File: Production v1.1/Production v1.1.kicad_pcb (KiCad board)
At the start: 2 copper layers, 35 x 30.2 mm, 39 parts, among them IC1 MAX3323EEUE+T, IC2 AP7375-33SA-7, J1 530480510, J13 FH34SRJ-16S-0.5SH_50_, J2 530480410, J3 USB4085-GF-A_REVB, U2 ADR02AUJZ-REEL7, U3 ATSAMD21G18A-AUT, Y1 ECS-.327-12.5-1210-TR

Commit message: Better v1.1, but I can do better
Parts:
- C13, C4, D1, D2, IC2: moved to B.Cu
- R1: moved to F.Cu
- RESET1: footprint Button_Switch_SMD:SW_SPST_B3U-1000P -> Button_Switch_SMD:SW_SPST_B3U-3000P
- moved J1 30.9 mm to (90.7, 90.2), turned to 90 degrees
- moved C3 29.1 mm to (119.5, 92.0), turned to 0 degrees
- moved J2 28.3 mm to (122.2, 85.2), turned to -90 degrees
- moved C1 28.3 mm to (120.5, 90.5), turned to 90 degrees
- moved C2 27.3 mm to (117.5, 92.0), turned to 180 degrees
- moved C5 25.8 mm to (115.5, 92.0), turned to 180 degrees
- moved U2 25.8 mm to (94.5, 88.8), turned to 90 degrees
- moved IC1 22.3 mm to (117.2, 87.5), turned to 90 degrees
- moved C4 15.3 mm to (112.8, 88.5), turned to 180 degrees
- moved D2 14.3 mm to (112.0, 92.0), turned to -90 degrees
- moved IC2 13.6 mm to (112.5, 85.8), turned to 0 degrees
- moved R3 11.0 mm to (101.0, 79.0)
- moved R5 11.0 mm to (101.0, 77.4)
- moved 3V3 11.0 mm to (128.8, 79.2)
- moved SWCLK 11.0 mm to (123.7, 79.2)
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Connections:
- U3 pad 16: unconnected-(U3-PA11-Pad16) -> ZSIG
- U3 pad 24: unconnected-(U3-PA15-Pad24) -> RUN
- U3 pad 39: RUN -> unconnected-(U3-PA27-Pad39)
- U3 pad 47: ZSIG -> unconnected-(U3-PB02-Pad47)
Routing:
- net GND: track 66.7 -> 15.8 mm, vias 20 -> 14
- net +3V3: track 66.3 -> 38.7 mm, vias 3 -> 1
- net SWDIO: track 14.0 -> 0.00 mm, vias 1 -> 0
- net SWCLK: track 10.1 -> 0.00 mm, vias 1 -> 0
- net +24V: track 38.5 -> 46.7 mm
- net Net-(J13-Pad4): track 8.50 -> 1.88 mm
- net RST: track 14.3 -> 20.6 mm
- net VIN: track 9.08 -> 4.18 mm
- net /Net-(J8-CC1): track 1.30 -> 5.67 mm
- net TIN1: track 8.97 -> 13.2 mm
- net SETBTN: track 19.0 -> 16.4 mm, vias 1 -> 0
- net VUSB: track 13.8 -> 11.9 mm
- net ROUT1: track 9.27 -> 11.2 mm
- net TOUT1: track 9.65 -> 8.29 mm
- net ZOOM: track 16.9 -> 15.6 mm
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- added copper zone on F.Cu, net GND
- added copper zone on B.Cu, net VIN
- removed copper zone on F.Cu, net VIN

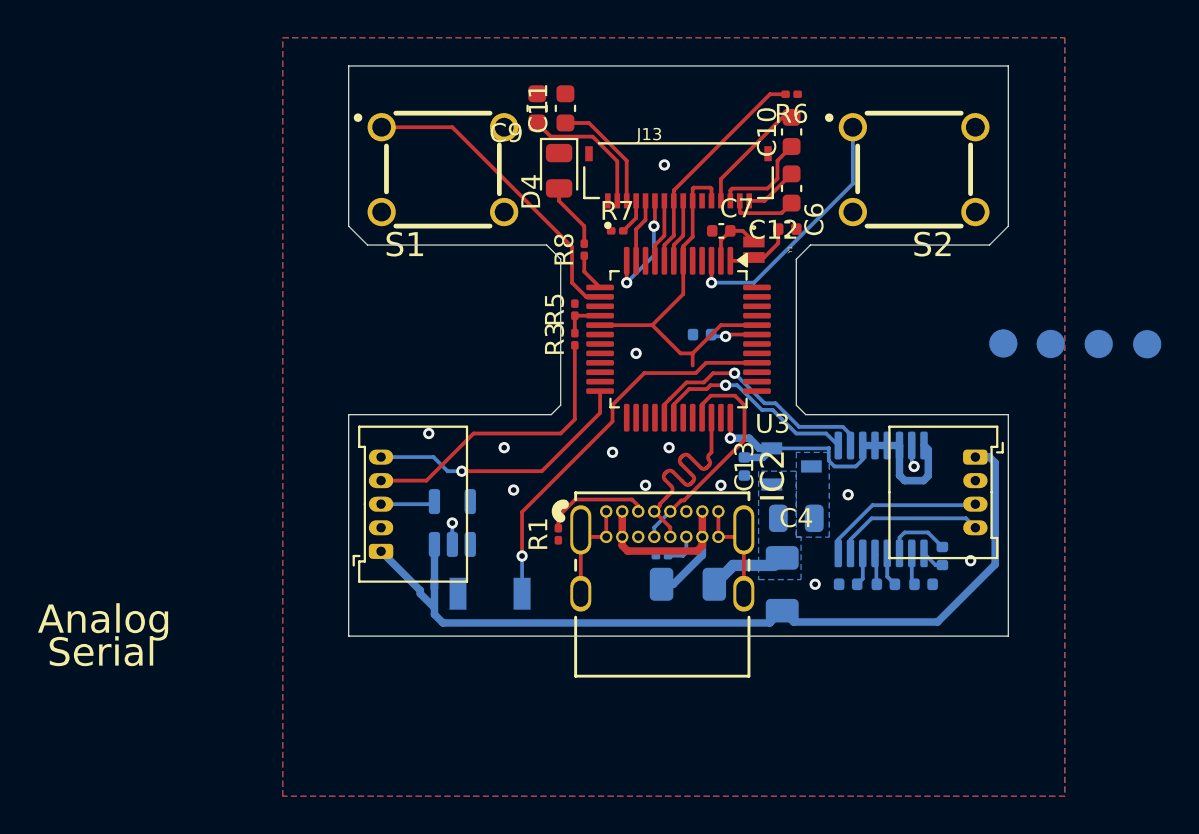
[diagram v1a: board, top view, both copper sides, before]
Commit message: Components are all moved to the bottom layer, top is ground
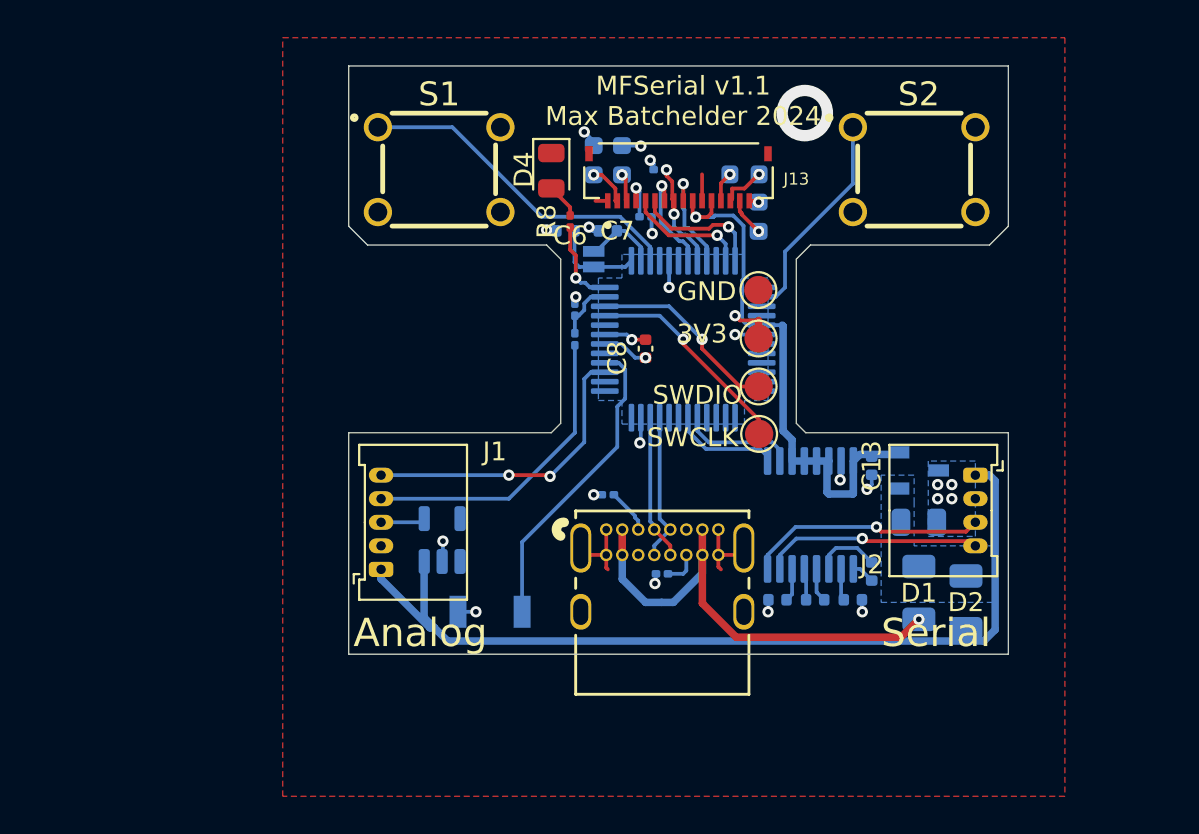
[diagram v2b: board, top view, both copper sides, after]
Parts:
- 3V3, C8, SWCLK, SWDIO: moved to F.Cu
- C10, C11, C12, C6, C7, C9, R1, R3, R5, R6, R7, U3, Y1: moved to B.Cu
- GND: renamed from G; moved to F.Cu
- moved GND 20.8 mm to (110.7, 76.4), turned to 0 degrees
- moved 3V3 18.0 mm to (110.8, 79.0), turned to 0 degrees
- moved SWDIO 15.7 mm to (110.8, 81.5), turned to 0 degrees
- moved SWCLK 13.8 mm to (110.8, 84.0), turned to 0 degrees
- moved D1 12.3 mm to (119.2, 92.5), turned to -90 degrees
- moved C6 11.8 mm to (100.5, 73.2), turned to 0 degrees
- moved D2 9.80 mm to (121.8, 93.0)
- moved Y1 8.51 mm to (102.0, 74.8)
- moved R6 8.06 mm to (105.5, 70.0), turned to 0 degrees
- moved IC2 6.75 mm to (119.2, 86.0)
- moved C13 6.75 mm to (116.8, 85.7)
- moved C4 6.50 mm to (119.2, 88.7)
- moved C7 6.02 mm to (102.8, 73.2)
- moved C11 4.07 mm to (103.5, 69.5)
- moved C9 4.07 mm to (102.0, 69.5)
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- renumbered RESET1 to S3
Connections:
- U3 pad 13: SETLED -> unconnected-(U3-PA08-Pad13)
- U3 pad 14: SETBTN -> SOFTBTN
- U3 pad 16: ZSIG -> unconnected-(U3-PA11-Pad16)
- U3 pad 24: RUN -> unconnected-(U3-PA15-Pad24)
- U3 pad 3: SOFTBTN -> SETBTN
- U3 pad 39: unconnected-(U3-PA27-Pad39) -> RUN
- U3 pad 47: unconnected-(U3-PB02-Pad47) -> ZSIG
- U3 pad 48: RXLED -> SETLED
- U3 pad 7: OLED_CS -> OLED_DC
- U3 pad 9: OLED_DC -> OLED_CS
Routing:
- net VUSB: track 11.9 -> 25.5 mm, vias 0 -> 1
- net GND: track 15.8 -> 27.2 mm, vias 14 -> 23
- net SWCLK: track 0.00 -> 11.4 mm, vias 0 -> 1
- net SWDIO: track 0.00 -> 10.2 mm, vias 0 -> 1
- net TIN1: track 13.2 -> 6.08 mm, vias 1 -> 0
- net OLED_RST: track 12.0 -> 5.66 mm, vias 0 -> 2
- net +3V3: track 38.7 -> 33.1 mm, vias 1 -> 2
- net ROUT1: track 11.2 -> 5.73 mm, vias 1 -> 0
- net Net-(C9-Pad2): track 7.19 -> 2.20 mm, vias 0 -> 1
- net Net-(C11-Pad1): track 6.21 -> 1.49 mm, vias 0 -> 1
- net Net-(C10-Pad2): track 6.26 -> 1.60 mm, vias 0 -> 1
- net D+: track 12.3 -> 7.72 mm
- net D-: track 12.4 -> 7.87 mm
- net RST: track 20.6 -> 16.4 mm, vias 1 -> 0
- net VIN: track 4.18 -> 0.00 mm
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- added copper zone on B.Cu, net +3V3
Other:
- board size 35 x 30.2 mm -> 35 x 31.2 mm
- board text added: "MFSerial v1.1 Max Batchelder 2024"
- board text removed: "MFSerial Production v1.1 Max Batchelder 2024"

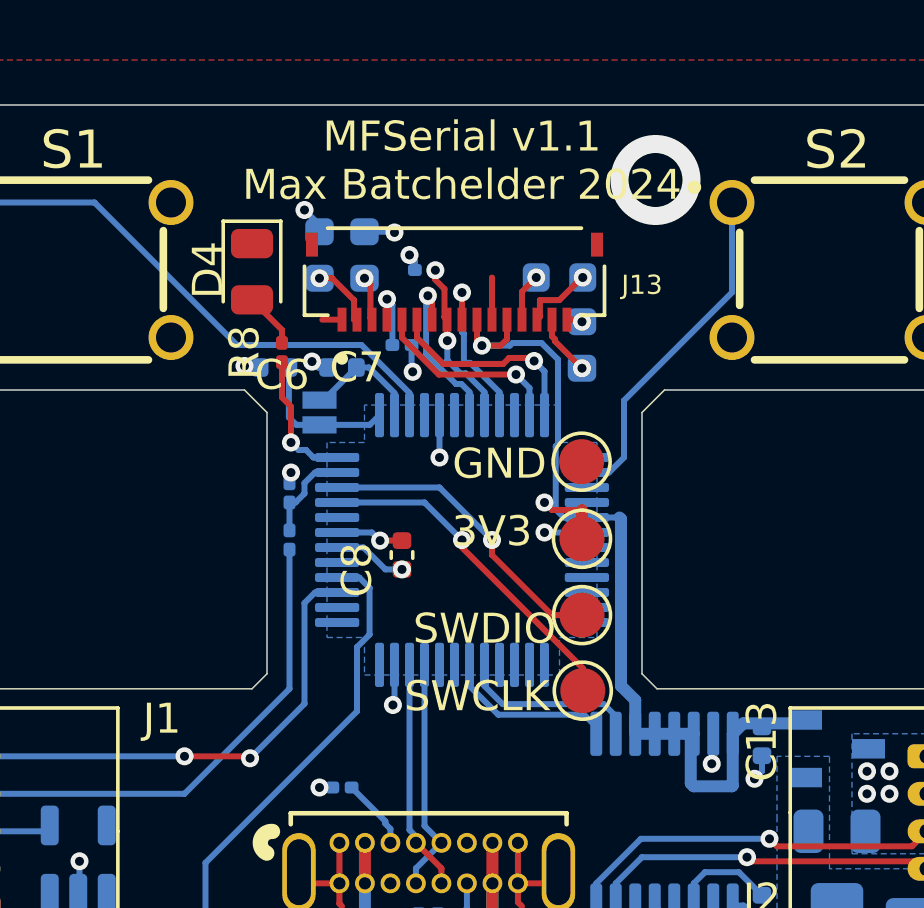
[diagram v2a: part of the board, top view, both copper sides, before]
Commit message: Solid v1.1, but I want to change how the oled is mounted.
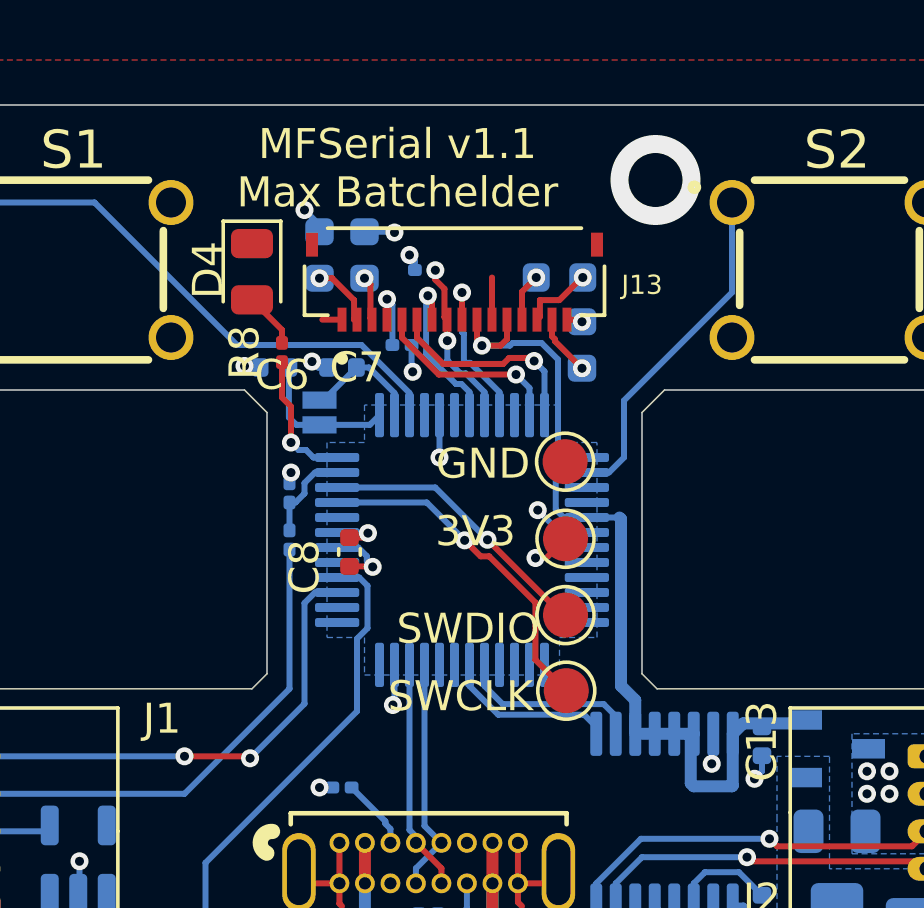
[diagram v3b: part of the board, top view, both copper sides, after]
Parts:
- S3: value B3U-1000P -> B3U-3000P
- moved C8 1.75 mm to (103.0, 79.4)
- moved GND 0.55 mm to (110.2, 76.4)
- moved 3V3 0.55 mm to (110.2, 79.0)
- moved SWCLK 0.55 mm to (110.2, 84.0)
- moved SWDIO 0.55 mm to (110.2, 81.5)
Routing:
- net +3V3: track 33.1 -> 32.0 mm
- net Net-(U3-VDDCORE): track 2.27 -> 1.71 mm
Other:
- board text added: "MFSerial v1.1 Max Batchelder"
- board text removed: "MFSerial v1.1 Max Batchelder 2024"

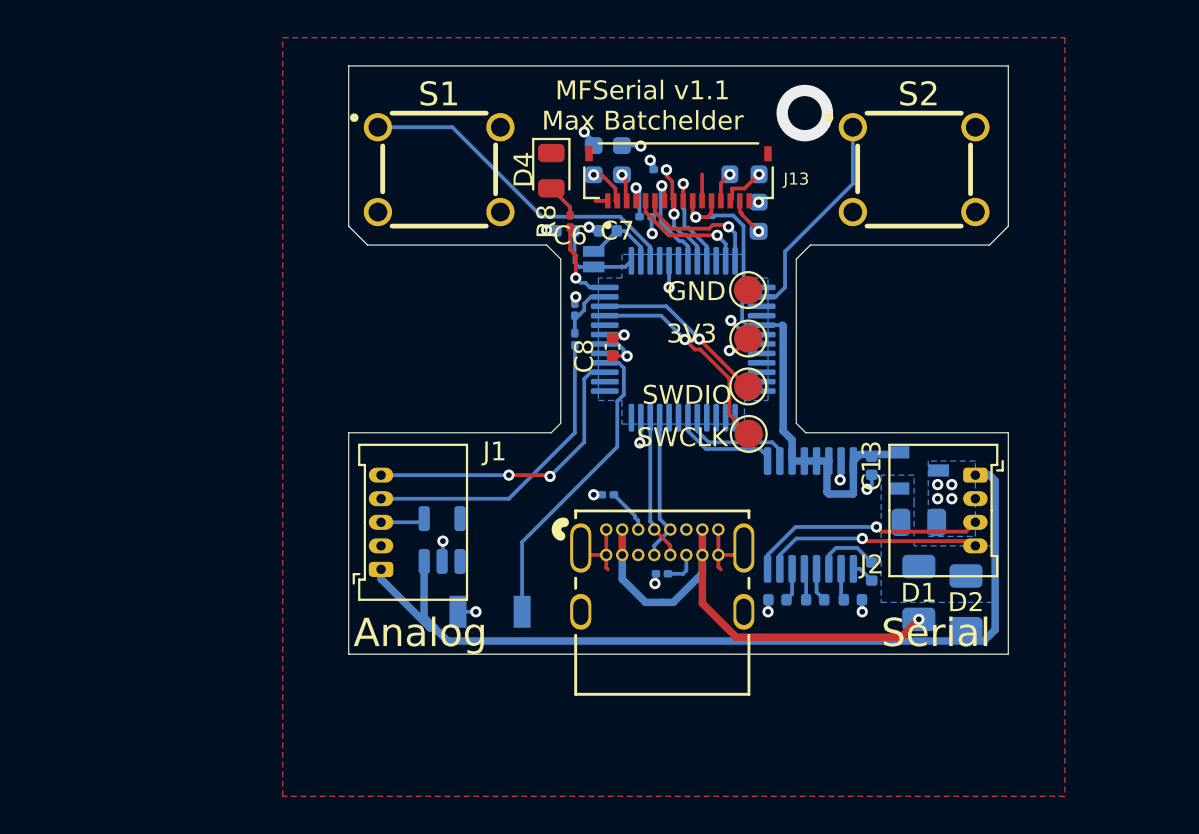
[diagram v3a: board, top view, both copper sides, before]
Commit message: v1.1 sent for assembly
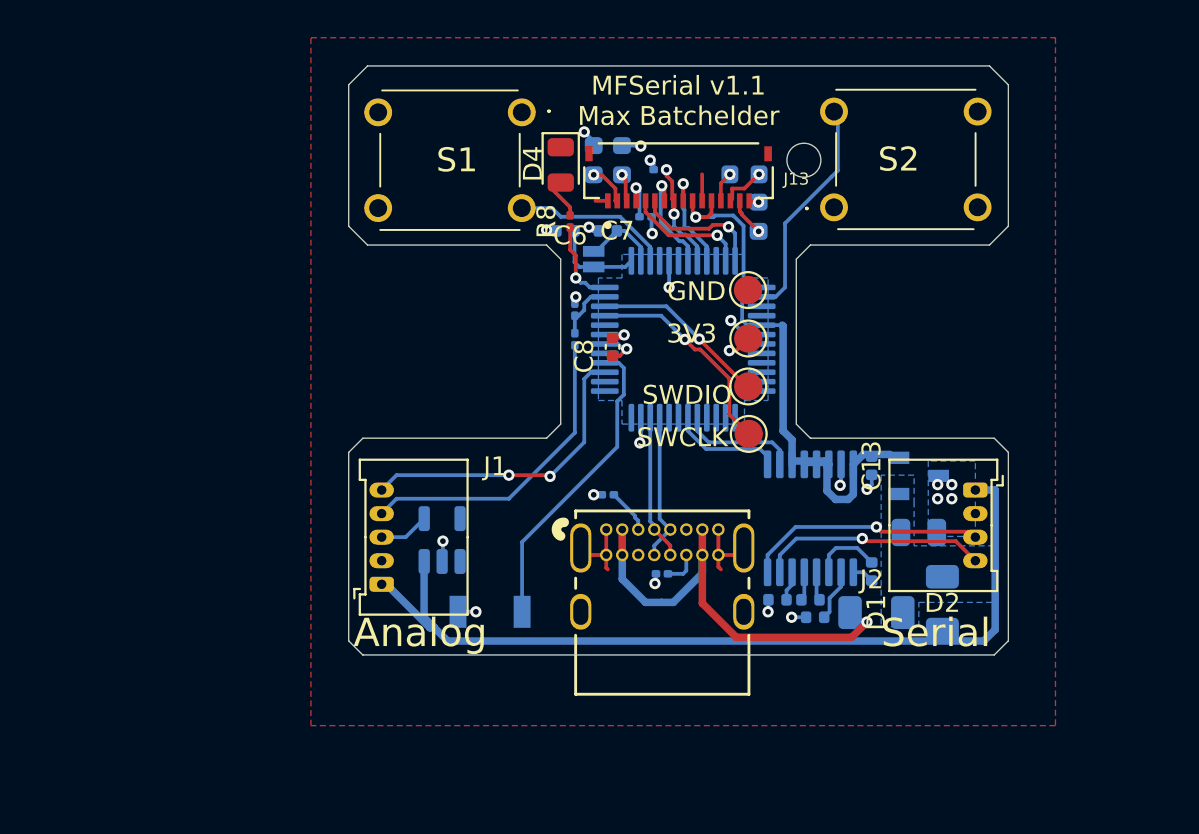
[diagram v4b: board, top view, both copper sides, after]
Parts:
- C13: value 10uF,10V+ -> 22uF,10V+
- C4: value 1uF,60V+ -> 2.2uF,100V
- S1, S2: value FSM12JH -> TL6100DF300QP; footprint FSM10JH:FSM4JH -> TL6100DF300QP:TL6100DF160QP
- moved S1 5.34 mm to (98.2, 67.0), turned to 180 degrees
- moved S2 4.70 mm to (114.8, 72.0)
- moved D1 2.48 mm to (117.0, 93.5), turned to 180 degrees
- moved C3 2.20 mm to (113.8, 93.8), turned to 180 degrees
- moved D2 1.25 mm to (120.5, 93.0)
- moved J1 0.79 mm to (90.8, 92.0)
- moved J2 0.79 mm to (122.2, 87.0)
- moved D4 0.59 mm to (100.2, 69.8)
- moved C4 0.54 mm to (119.2, 89.2)
- moved IC2 0.29 mm to (119.2, 86.2)
- moved C2 0.25 mm to (113.5, 92.8)
- moved IC1 0.18 mm to (113.5, 88.5)
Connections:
- S1 pad 1: SETBTN -> GND
- S1 pad 3: GND -> SETBTN
- S2 pad 1: SOFTBTN -> GND
- S2 pad 3: GND -> SOFTBTN
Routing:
- net SETBTN: track 17.8 -> 8.41 mm
- net VUSB: track 25.5 -> 23.8 mm
- net +24V: track 47.5 -> 46.3 mm
- net /Net-(IC1-V+): track 1.70 -> 2.76 mm
- net +3V3: track 32.0 -> 33.0 mm
- net TOUT1: track 11.6 -> 12.1 mm
- net (no net): vias 1 -> 0
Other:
- outline, holes or cut-outs redrawn

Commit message: Updated v1.1 and re-ordered
One net was not connected
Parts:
- moved C2 0.16 mm to (113.7, 92.8)
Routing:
- net RUN: track 16.4 -> 16.6 mm, vias 2 -> 1

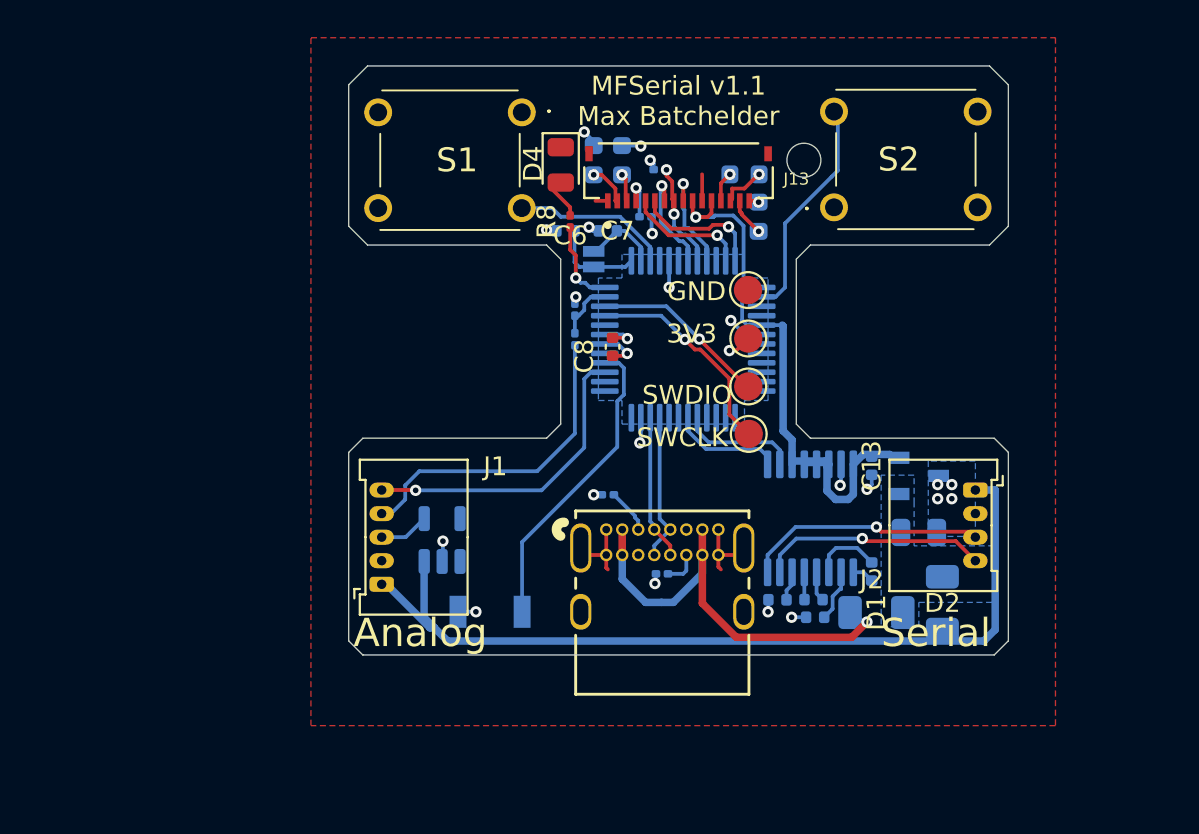
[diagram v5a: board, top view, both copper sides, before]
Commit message: Resubmitted again, no more vias in pads
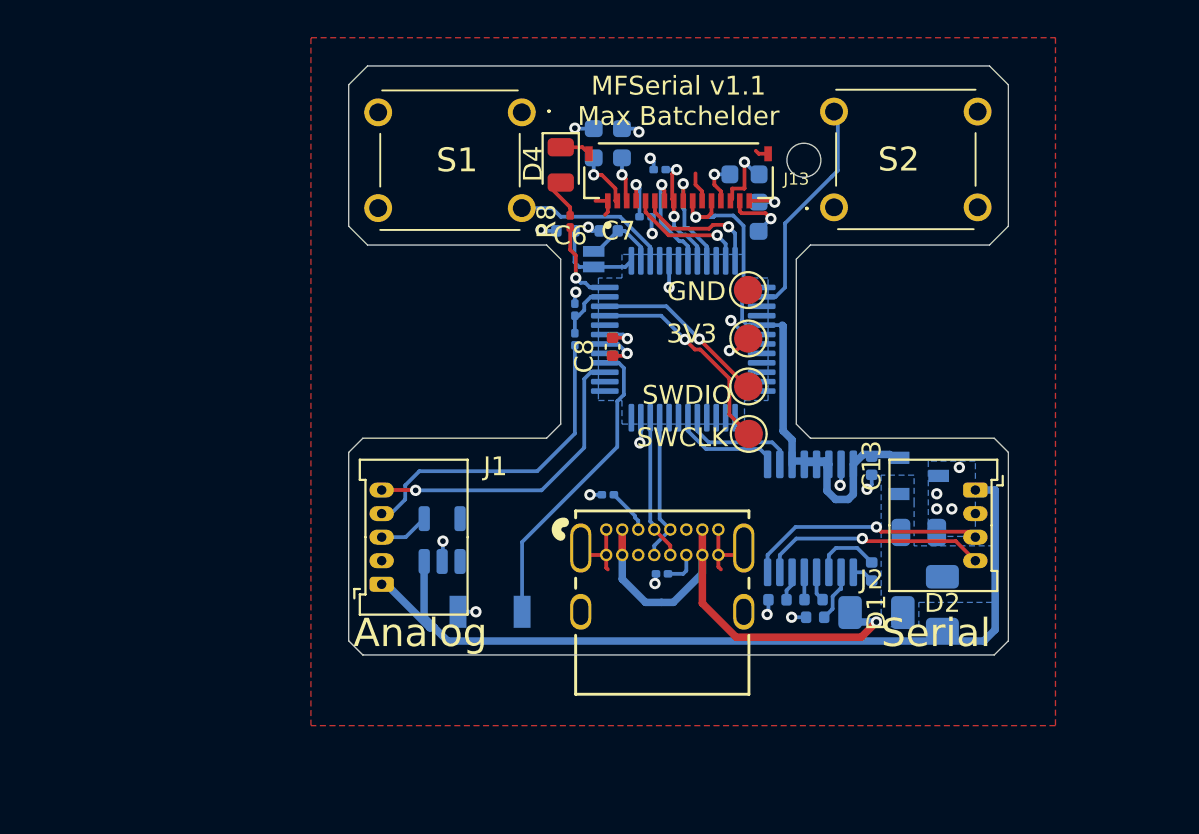
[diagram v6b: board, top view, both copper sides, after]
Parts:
- moved C11 0.90 mm to (103.5, 68.6)
- moved C9 0.90 mm to (102.0, 68.6)
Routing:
- net GND: track 27.7 -> 32.2 mm
- net Net-(C12-Pad1): track 0.53 -> 2.23 mm
- net Net-(C10-Pad1): track 2.43 -> 3.79 mm
- net Net-(C12-Pad2): track 2.03 -> 3.31 mm
- net VUSB: track 23.8 -> 24.8 mm
- net Net-(C9-Pad2): track 2.20 -> 3.10 mm
- net Net-(C11-Pad1): track 1.49 -> 2.39 mm
- net Net-(C10-Pad2): track 1.60 -> 2.38 mm
- net OLED_RST: track 5.66 -> 6.17 mm
